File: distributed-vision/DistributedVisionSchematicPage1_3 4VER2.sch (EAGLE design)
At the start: 150 parts, among them J1 USBR-A-D-F-O-TH, J12 ARJM11C7-104-AB-EW2, J2 RASPBERRRY_COMPUTE_CM3, J6 DM3D-SF, J8 1-84952-5, J9 1-84952-5, Q7 25 MHz, U1 LM26420XMH, U11 IFX91041, U12 TPS26600PWPR, U3 LAN9513-JZXQFN64_9X9MC_MCH-M, U8 SP3003-02, U9 SP3003-02, X1 JST-XH-02-PIN-LONG-PAD

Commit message: Joe Cleanup Schematic
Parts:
- removed C53: 100n, rcl:C-USC0402
- removed R2: (no value), rcl:R-US_R0603
- removed R31: 4.7k, RoboJackets-Resistors:ERJ-L06KF50MV
- F2: value 1A (Trip) -> 2A; device ethernet_poe:0ZCG0050AF2C -> RoboJackets-Fuses:PTCFUSE-1812
- R26: value 12k -> 12k, 1.0%
- R27: value 12.4k -> 12.4k, 1.0%
- R7: value 5r1 -> 5.1
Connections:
- removed net BD+: J1.D1+, U9.IO2
- removed net N$61: C53.1, R31.PIN1, U3.NRESET
- removed net USBDM3: U3.USBDM3
- removed net USBDP2: U3.USBDP2
- removed net USBDP3: J1.D2+, J1.D2-, U3.USBDP3, U8.IO1, U8.IO2
- removed net USB_DM: U3.USBDM0
- removed net USB_DP: U3.USBDP0
- removed net USB_OTGID: J2A.USB_OTGID, R2.2
- removed net VBATT: C18.1, C19.1, C21.1, C22.1, C35.1, J2B.VBAT@1, J2B.VBAT@2, J2B.VBAT@3, J2B.VBAT@4
- new net N$12: U8.IO1
- new net N$3: R13.2, U1.FB1
- new net N$6: U9.IO2
- new net N$7: U8.IO2
- new net RX_P1: R9.2, U1.PGND_2
- new net USB0_N: J2A.USB_DM, U3.USBDM0
- new net USB0_P: J2A.USB_DP, U3.USBDP0
- new net USB2_N: J1.D1-, U3.USBDM2
- new net USB2_P: J1.D1+, U3.USBDP2
- new net USB3_N: J1.D2-, U3.USBDM3
- new net USB3_P: J1.D2+, U3.USBDP3
- net +3.3V: now also U3.NRESET; no longer R31.PIN2
- net +5V: now also C18.1, C19.1, C21.1, C22.1, C35.1, J2B.VBAT@1, J2B.VBAT@2, J2B.VBAT@3, J2B.VBAT@4
- net BVCC: no longer J1.VCC1
- net GND: now also J1.SHIELD, J2A.USB_OTGID; no longer C53.2, R2.1
- net RX_P: no longer R9.2, U1.PGND_2
- net TVCC: now also J1.VCC1
- net USBDM2: no longer J1.D1-, U3.USBDM2
- net VDD18CORE: no longer R13.2, U1.FB1
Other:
- note removed: "CM1 VBAT = 3v3"
- note removed: "SELECT VBAT for CM1 or CM3"
- moved on the sheet: C23, C75, C86, R13, R14, R28

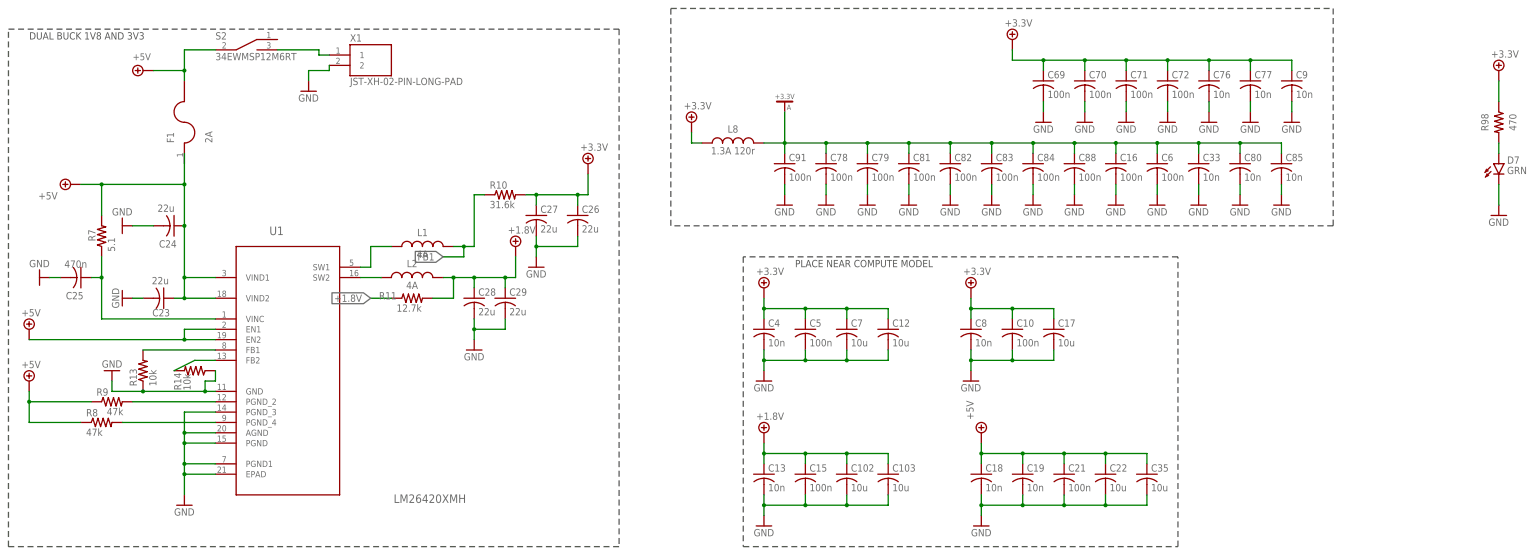
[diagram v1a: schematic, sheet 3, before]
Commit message: Updated Values in DisbVision sch
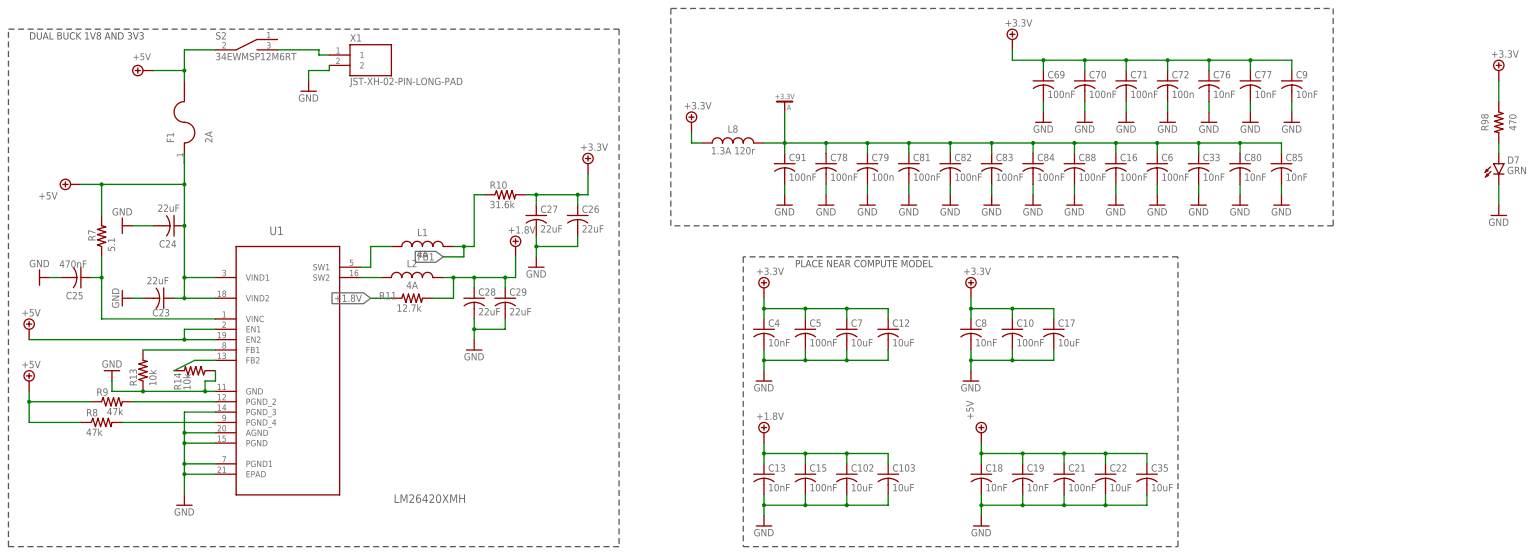
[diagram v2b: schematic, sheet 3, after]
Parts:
- C10, C15, C16, C21, C42, C45, C46, C5, C50, C6, C60, C63, C68, C69, C70, C71, C78, C81, C82, C83, C84, C88, C91: value 100n -> 100nF
- C102, C103, C12, C17, C22, C35, C7, C73: value 10u -> 10uF
- C13, C18, C19, C20, C33, C4, C51, C52, C58, C61, C75, C76, C77, C8, C80, C85, C86, C9: value 10n -> 10nF
- C14, C64: value 1u -> 1uF
- C23, C24, C26, C27, C28, C29: value 22u -> 22uF
- C25: value 470n -> 470nF
- C43, C44, C62: value 4u7 -> 4.7uF
- C65, C66: value 33p -> 33pF

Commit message: Routed Board Based off Schematic Changes
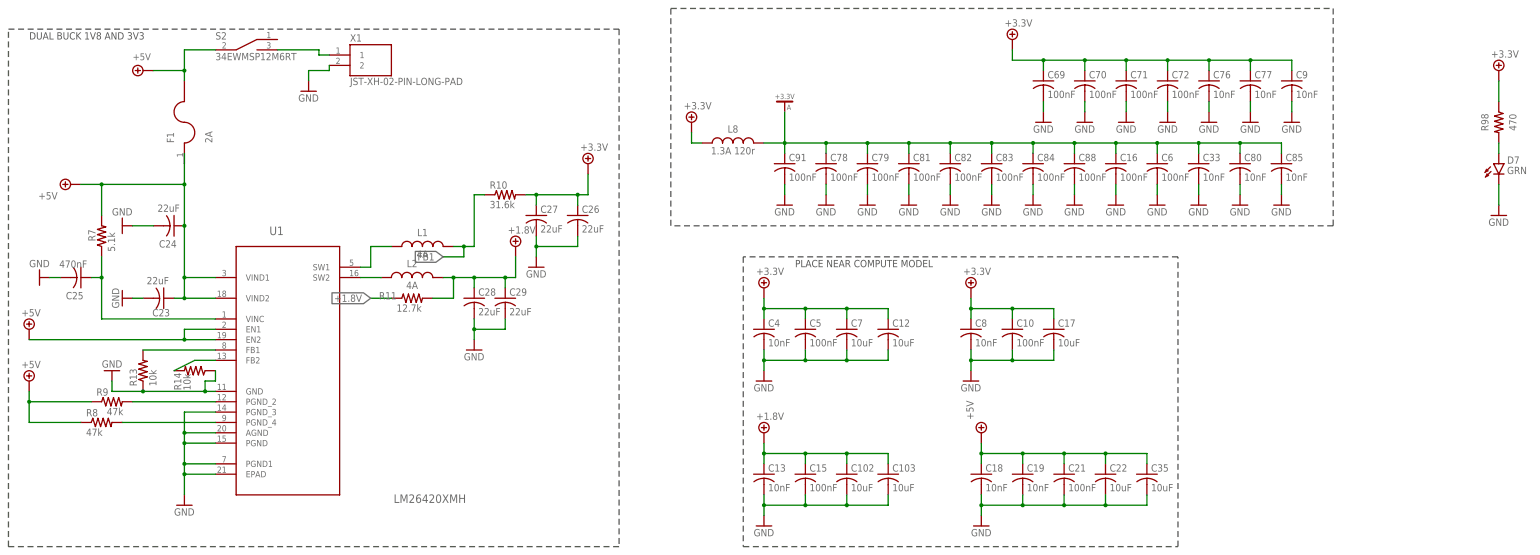
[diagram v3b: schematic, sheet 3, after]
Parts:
- C72, C79: value 100n -> 100nF
- R7: value 5.1 -> 5.1k
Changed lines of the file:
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@@
 <part name="C91" library="rcl" library_urn="urn:adsk.eagle:library:334" deviceset="C-US" device="C0603" package3d_urn="urn:adsk.eagle:package:23616/2" value="100nF"/>
 <part name="C78" library="rcl" library_urn="urn:adsk.eagle:library:334" deviceset="C-US" device="C0603" package3d_urn="urn:adsk.eagle:package:23616/2" value="100nF"/>
-<part name="C79" library="rcl" library_urn="urn:adsk.eagle:library:334" deviceset="C-US" device="C0603" package3d_urn="urn:adsk.eagle:package:23616/2" value="100n"/>
+<part name="C79" library="rcl" library_urn="urn:adsk.eagle:library:334" deviceset="C-US" device="C0603" package3d_urn="urn:adsk.eagle:package:23616/2" value="100nF"/>
 <part name="C81" library="rcl" library_urn="urn:adsk.eagle:library:334" deviceset="C-US" device="C0603" package3d_urn="urn:adsk.eagle:package:23616/2" value="100nF"/>
 <part name="C82" library="rcl" library_urn="urn:adsk.eagle:library:334" deviceset="C-US" device="C0603" package3d_urn="urn:adsk.eagle:package:23616/2" value="100nF"/>
@@
 <part name="C70" library="rcl" library_urn="urn:adsk.eagle:library:334" deviceset="C-US" device="C0603" package3d_urn="urn:adsk.eagle:package:23616/2" value="100nF"/>
 <part name="C71" library="rcl" library_urn="urn:adsk.eagle:library:334" deviceset="C-US" device="C0603" package3d_urn="urn:adsk.eagle:package:23616/2" value="100nF"/>
-<part name="C72" library="rcl" library_urn="urn:adsk.eagle:library:334" deviceset="C-US" device="C0603" package3d_urn="urn:adsk.eagle:package:23616/2" value="100n"/>
+<part name="C72" library="rcl" library_urn="urn:adsk.eagle:library:334" deviceset="C-US" device="C0603" package3d_urn="urn:adsk.eagle:package:23616/2" value="100nF"/>
 <part name="C76" library="rcl" library_urn="urn:adsk.eagle:library:334" deviceset="C-US" device="C0603" package3d_urn="urn:adsk.eagle:package:23616/2" value="10nF"/>
 <part name="C77" library="rcl" library_urn="urn:adsk.eagle:library:334" deviceset="C-US" device="C0603" package3d_urn="urn:adsk.eagle:package:23616/2" value="10nF"/>
@@
 <part name="C24" library="rcl" library_urn="urn:adsk.eagle:library:334" deviceset="C-US" device="C0603" package3d_urn="urn:adsk.eagle:package:23616/2" value="22uF"/>
 <part name="C25" library="rcl" library_urn="urn:adsk.eagle:library:334" deviceset="C-US" device="C0603" package3d_urn="urn:adsk.eagle:package:23616/2" value="470nF"/>
-<part name="R7" library="rcl" library_urn="urn:adsk.eagle:library:334" deviceset="R-US_" device="R0603" package3d_urn="urn:adsk.eagle:package:23555/3" value="5.1"/>
+<part name="R7" library="rcl" library_urn="urn:adsk.eagle:library:334" deviceset="R-US_" device="R0603" package3d_urn="urn:adsk.eagle:package:23555/3" value="5.1k"/>
 <part name="R13" library="rcl" library_urn="urn:adsk.eagle:library:334" deviceset="R-US_" device="R0603" package3d_urn="urn:adsk.eagle:package:23555/3" value="10k"/>
 <part name="R14" library="rcl" library_urn="urn:adsk.eagle:library:334" deviceset="R-US_" device="R0603" package3d_urn="urn:adsk.eagle:package:23555/3" value="10k"/>

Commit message: BOM/PnP Changes
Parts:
- R40: value 4k7 -> 4.7k
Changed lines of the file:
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@@
 <part name="SUPPLY132" library="RoboJackets-Supplies" deviceset="GND" device=""/>
 <part name="SUPPLY133" library="RoboJackets-Supplies" deviceset="GND" device=""/>
-<part name="R40" library="RoboJackets-Resistors" deviceset="ERJ-L06KF50MV" device="" value="4k7"/>
+<part name="R40" library="RoboJackets-Resistors" deviceset="ERJ-L06KF50MV" device="" value="4.7k"/>
 <part name="R39" library="RoboJackets-Resistors" deviceset="ERJ-L06KF50MV" device="" value="1M"/>
 <part name="C66" library="rcl" library_urn="urn:adsk.eagle:library:334" deviceset="C-US" device="C0402" package3d_urn="urn:adsk.eagle:package:23626/2" value="33pF"/>
